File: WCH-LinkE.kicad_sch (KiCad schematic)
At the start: 35 parts, among them J2 Conn_02x05_Odd_Even, J3 USB_C_Receptacle_USB2.0_16P, SW1 SW_Push, SW2 SW_Push, U1 AMS1117-3.3, U2 CH32V305FBP6, U3 CH217K, U4 CH217K, Y2 12M

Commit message: csv position fix
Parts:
- J3: JLCPCB Position Offset 0, 0.13 -> 0, 1.05
- U1: JLCPCB Position Offset (none) -> -0.6, 0
- U3, U4: footprint Package_TO_SOT_SMD:SOT-23-6 -> Package_TO_SOT_SMD:SOT-23-6_Handsoldering
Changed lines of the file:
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@@
 			)
 		)
-		(property "Footprint" "Package_TO_SOT_SMD:SOT-23-6"
+		(property "Footprint" "Package_TO_SOT_SMD:SOT-23-6_Handsoldering"
 			(at 111.76 110.49 0)
 			(effects
@@
 			)
 		)
-		(property "JLCPCB Position Offset" "0, 0.13"
+		(property "JLCPCB Position Offset" "0, 1.05"
 			(at 52.07 59.69 0)
 			(effects
@@
 			)
 		)
+		(property "JLCPCB Position Offset" "-0.6, 0"
+			(at 102.87 44.45 0)
+			(effects
+				(font
+					(size 1.27 1.27)
+				)
+				(hide yes)
+			)
+		)
 		(pin "1"
 		)
@@
 			)
 		)
-		(property "Footprint" "Package_TO_SOT_SMD:SOT-23-6"
+		(property "Footprint" "Package_TO_SOT_SMD:SOT-23-6_Handsoldering"
 			(at 111.76 139.7 0)
 			(effects

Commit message: move ch217k
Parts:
- removed U1: AMS1117-3.3, Package_TO_SOT_SMD:SOT-89-3, symbol Regulator_Linear:AMS1117-3.3
- added U1: RT9080-33GJ5, Package_TO_SOT_SMD:TSOT-23-5, symbol Regulator_Linear:SPX3819M5-L-3-3
- C2: value 10u -> 1u; footprint Capacitor_SMD:C_0603_1608Metric -> Capacitor_SMD:C_0402_1005Metric; LCSC C96446 -> C52923
- C4: value 22u -> 10u; footprint Capacitor_SMD:C_0603_1608Metric -> Capacitor_SMD:C_0402_1005Metric; LCSC C59461 -> C15525
- J3: JLCPCB Position Offset 0, 1.05 -> 0, 1.3
- U3, U4: footprint Package_TO_SOT_SMD:SOT-23-6_Handsoldering -> Package_TO_SOT_SMD:SOT-23-6; JLCPCB Rotation Offset (none) -> 90
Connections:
- net +3V3: now also U1.5 (OUT)
- net +5V: now also U1.1 (IN), U1.3 (EN)
- net GND: now also U1.2 (GND)
- no-connect marks 4 -> 5
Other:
- moved on the sheet: C4, D2, R8

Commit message: position fix
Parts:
- J3: footprint Connector_USB:USB_C_Receptacle_XKB_U262-16XN-4BVC11 -> Connector_USB:USB_C_Receptacle_G-Switch_GT-USB-7010ASV; JLCPCB Position Offset 0, 1.3 -> 0, 1.36; LCSC C2988369 -> C393939
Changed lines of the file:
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@@
 			)
 		)
-		(property "Footprint" "Connector_USB:USB_C_Receptacle_XKB_U262-16XN-4BVC11"
+		(property "Footprint" "Connector_USB:USB_C_Receptacle_G-Switch_GT-USB-7010ASV"
 			(at 55.88 59.69 0)
 			(effects
@@
 			)
 		)
-		(property "LCSC" "C2988369"
+		(property "LCSC" "C393939"
 			(at 52.07 59.69 0)
 			(effects
@@
 			)
 		)
-		(property "JLCPCB Position Offset" "0, 1.3"
+		(property "JLCPCB Position Offset" "0, 1.36"
 			(at 52.07 59.69 0)
 			(effects

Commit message: version fix and show previous version
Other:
- title: WCH-LinkE -> WCH-LinkE Clone
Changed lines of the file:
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@@
 	(paper "A4")
 	(title_block
-		(title "WCH-LinkE")
-		(rev "v1.0.0")
+		(title "WCH-LinkE Clone")
+		(rev "v1.1.0")
 	)
 	(junction

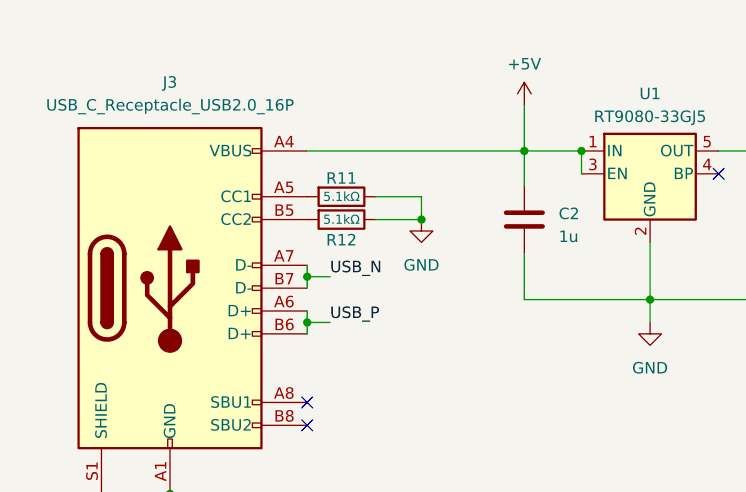
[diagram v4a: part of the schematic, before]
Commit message: fix trace for gnd
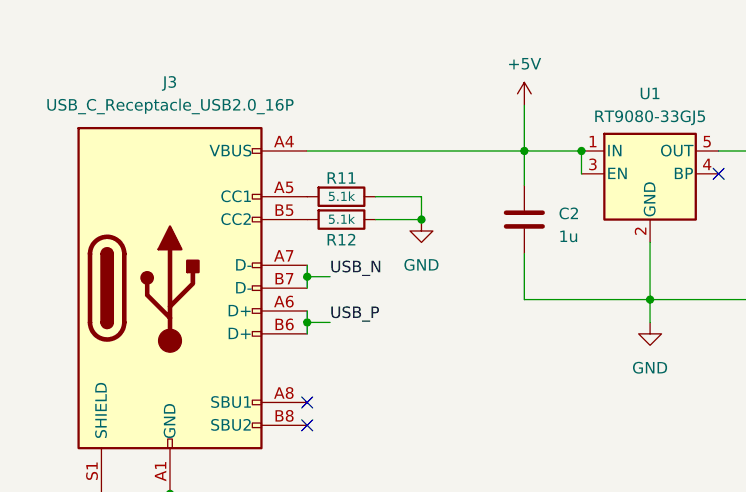
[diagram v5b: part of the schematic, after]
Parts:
- R11, R12: value 5.1kΩ -> 5.1k
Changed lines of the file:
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@@
 			)
 		)
-		(property "Value" "5.1kΩ"
+		(property "Value" "5.1k"
 			(at 71.12 49.53 90)
 			(effects
@@
 			)
 		)
-		(property "Value" "5.1kΩ"
+		(property "Value" "5.1k"
 			(at 71.12 52.07 90)
 			(effects

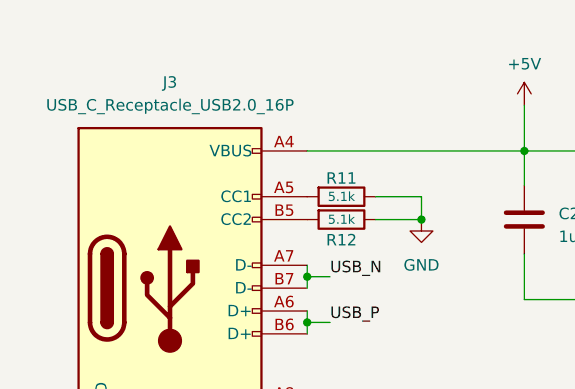
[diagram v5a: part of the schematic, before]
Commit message: fix library and fillzone
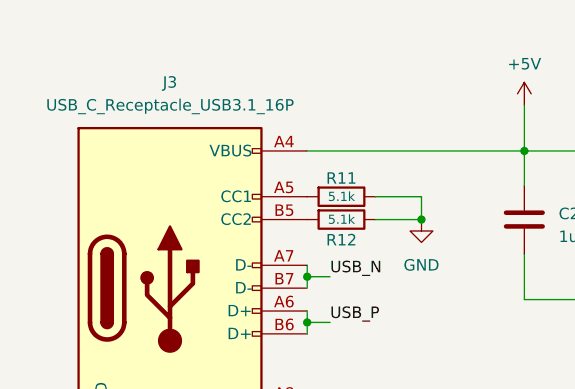
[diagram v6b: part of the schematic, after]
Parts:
- J3: value USB_C_Receptacle_USB2.0_16P -> USB_C_Receptacle_USB3.1_16P; footprint Connector_USB:USB_C_Receptacle_G-Switch_GT-USB-7010ASV -> USB:USB_C_Receptacle; JLCPCB Position Offset 0, 1.36 -> 0, 1.02
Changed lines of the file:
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@@
 			)
 		)
-		(property "Value" "USB_C_Receptacle_USB2.0_16P"
+		(property "Value" "USB_C_Receptacle_USB3.1_16P"
 			(at 52.07 39.37 0)
 			(effects
@@
 			)
 		)
-		(property "Footprint" "Connector_USB:USB_C_Receptacle_G-Switch_GT-USB-7010ASV"
+		(property "Footprint" "USB:USB_C_Receptacle"
 			(at 55.88 59.69 0)
 			(effects
@@
 			)
 		)
-		(property "Description" "USB 2.0-only 16P Type-C Receptacle connector"
+		(property "Description" "USB 3.1-only 16P Type-C Receptacle connector"
 			(at 52.07 59.69 0)
 			(effects
@@
 			)
 		)
-		(property "JLCPCB Position Offset" "0, 1.36"
+		(property "JLCPCB Position Offset" "0, 1.02"
 			(at 52.07 59.69 0)
 			(effects

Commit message: v1.1.0 pre-release
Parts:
- removed U1: RT9080-33GJ5, Package_TO_SOT_SMD:TSOT-23-5, symbol Regulator_Linear:SPX3819M5-L-3-3
- removed U3, U4: CH217K, Package_TO_SOT_SMD:SOT-23-6, symbol CH217K:CH217K
- added C6: 0.1u, Capacitor_SMD:C_0402_1005Metric, symbol Device:C
- added D3: 1N5819WS, Diode_SMD:D_SOD-323, symbol Diode:1N5819WS
- added Q1, Q2, Q3: AO3401A, Package_TO_SOT_SMD:SOT-23, symbol Transistor_FET:AO3401A
- added U5: XC6206P332MR-G, Package_TO_SOT_SMD:SOT-23-3, symbol Regulator_Linear:XC6206PxxxMR
- C4: value 10u -> 1u; LCSC C15525 -> C52923
- C5: value 100n -> 0.1u
- J3: value USB_C_Receptacle_USB3.1_16P -> TYPE-C16PIN
- R13: value 150k -> 47k; footprint Resistor_SMD:R_0603_1608Metric -> Resistor_SMD:R_0402_1005Metric; LCSC C22807 -> C25792
- R14: value 300k -> 100k; footprint Resistor_SMD:R_0603_1608Metric -> Resistor_SMD:R_0402_1005Metric; LCSC C23024 -> C25741
- R8, R9: value 1k -> 5.1k; LCSC C11702 -> C25905
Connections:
- net +3V3: now also Q1.2 (S), U5.2 (VO)
- net +5V: now also R13.1, C6.1, D3.2 (A), Q2.2 (S); no longer C2.1
- net 3V3_OUT: now also Q1.3 (D)
- net 5V_OUT: now also Q2.3 (D)
- net GND: now also Q3.3 (D), U5.1 (GND); no longer R13.2, R14.2
- net PA5: now also Q1.1 (G)
- net PB12: now also Q3.1 (G)
- net at R14.1: now also R13.2, C6.2, Q2.1 (G)
- new net: Q3.2 (S), R14.2
- new net: C2.1, D3.1 (K), U5.3 (VI)
- no-connect marks 5 -> 2
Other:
- moved on the sheet: H2, J2, J3, R11, R12

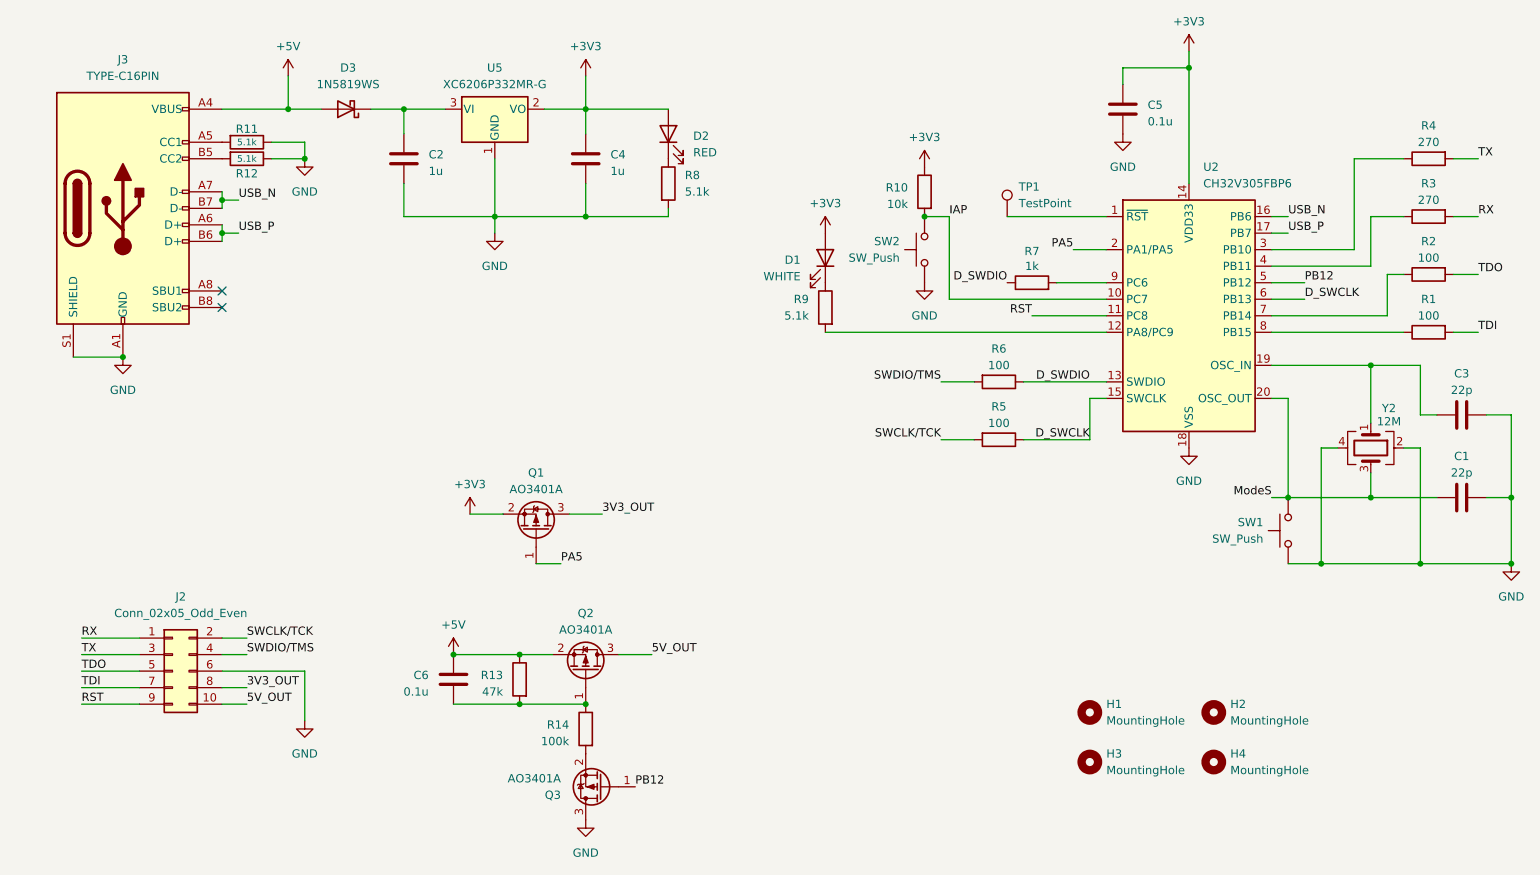
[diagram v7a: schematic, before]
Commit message: fix resistor value
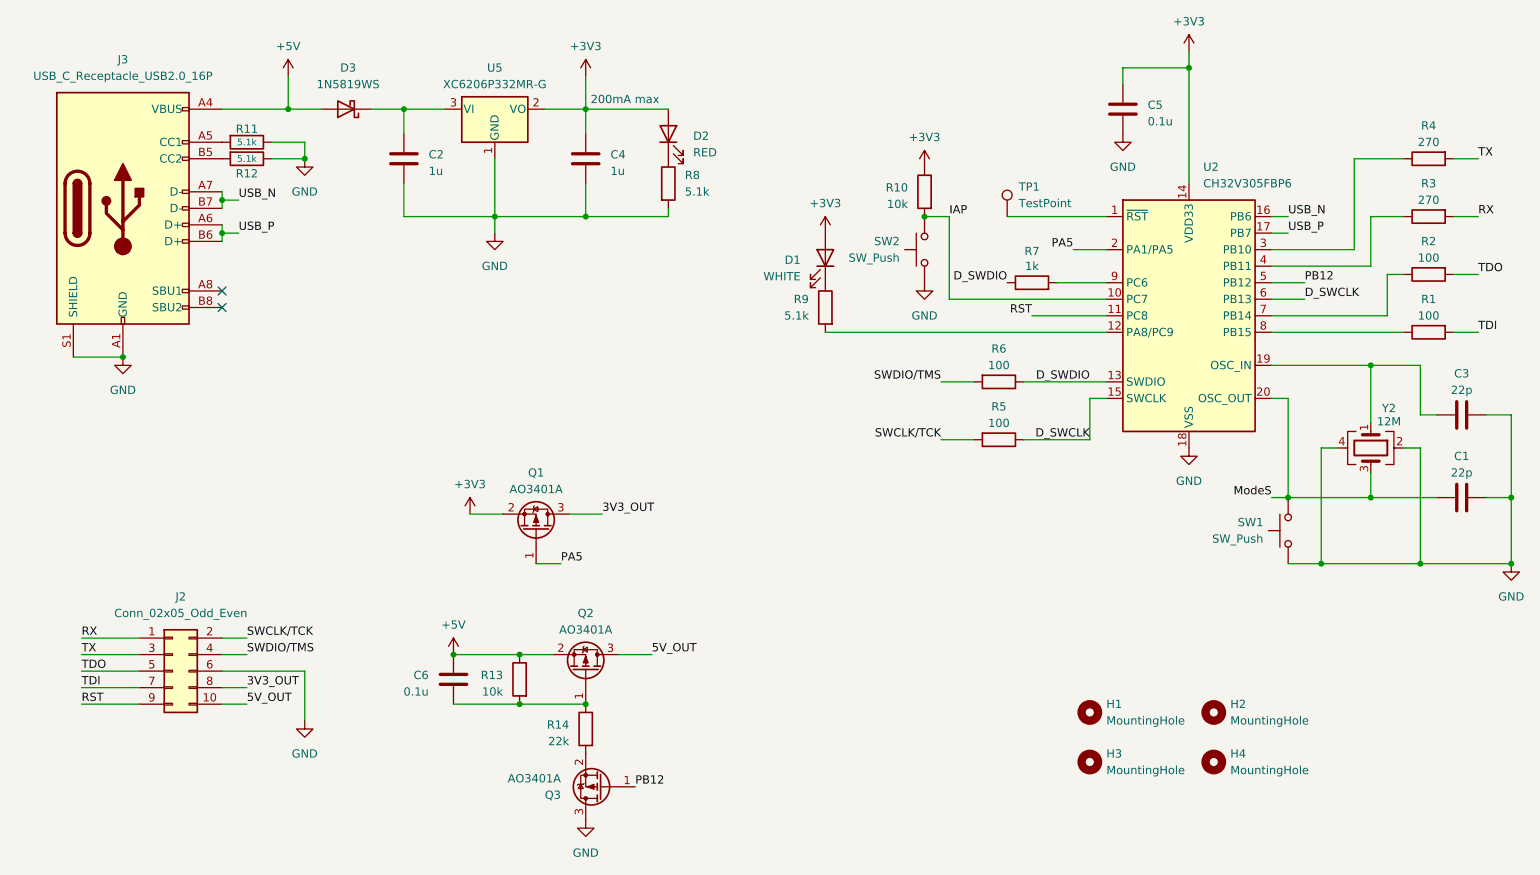
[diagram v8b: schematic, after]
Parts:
- J3: value TYPE-C16PIN -> USB_C_Receptacle_USB2.0_16P; LCSC C393939 -> C2988369
- R13: value 47k -> 10k; LCSC C25792 -> C25744
- R14: value 100k -> 22k; LCSC C25741 -> C25768
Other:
- note added: "200mA max"
- title: WCH-LinkE Clone -> WCH-LinkE-Mini
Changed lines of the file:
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@@
 	(paper "A4")
 	(title_block
-		(title "WCH-LinkE Clone")
+		(title "WCH-LinkE-Mini")
 		(rev "v1.1.0")
 	)
@@
 		)
 	)
+	(text "200mA max"
+		(exclude_from_sim no)
+		(at 120.142 43.18 0)
+		(effects
+			(font
+				(size 1.27 1.27)
+			)
+			(justify left)
+		)
+	)
 	(label "D_SWDIO"
 		(at 184.15 71.12 180)
@@
 			)
 		)
-		(property "Value" "47k"
+		(property "Value" "10k"
 			(at 106.68 133.985 0)
 			(effects
@@
 			)
 		)
-		(property "LCSC" "C25792"
+		(property "LCSC" "C25744"
 			(at 109.22 132.08 0)
 			(effects
@@
 			)
 		)
-		(property "Value" "TYPE-C16PIN"
+		(property "Value" "USB_C_Receptacle_USB2.0_16P"
 			(at 48.26 39.37 0)
 			(effects
@@
 			)
 		)
-		(property "Description" "USB 3.1-only 16P Type-C Receptacle connector"
+		(property "Description" "USB 2.0-only 16P Type-C Receptacle connector"
 			(at 48.26 59.69 0)
 			(effects
@@
 			)
 		)
-		(property "LCSC" "C393939"
+		(property "LCSC" "C2988369"
 			(at 48.26 59.69 0)
 			(effects
@@
 			)
 		)
-		(property "Value" "100k"
+		(property "Value" "22k"
 			(at 116.84 141.605 0)
 			(effects
@@
 			)
 		)
-		(property "LCSC" "C25741"
+		(property "LCSC" "C25768"
 			(at 119.38 139.7 0)
 			(effects
